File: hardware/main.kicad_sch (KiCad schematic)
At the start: 19 parts, among them J1 Conn_01x04, J2 M300-MV10345M1, J4 ScrewTerminal, J5 ScrewTerminal, J6 ScrewTerminal, K2 ADW11

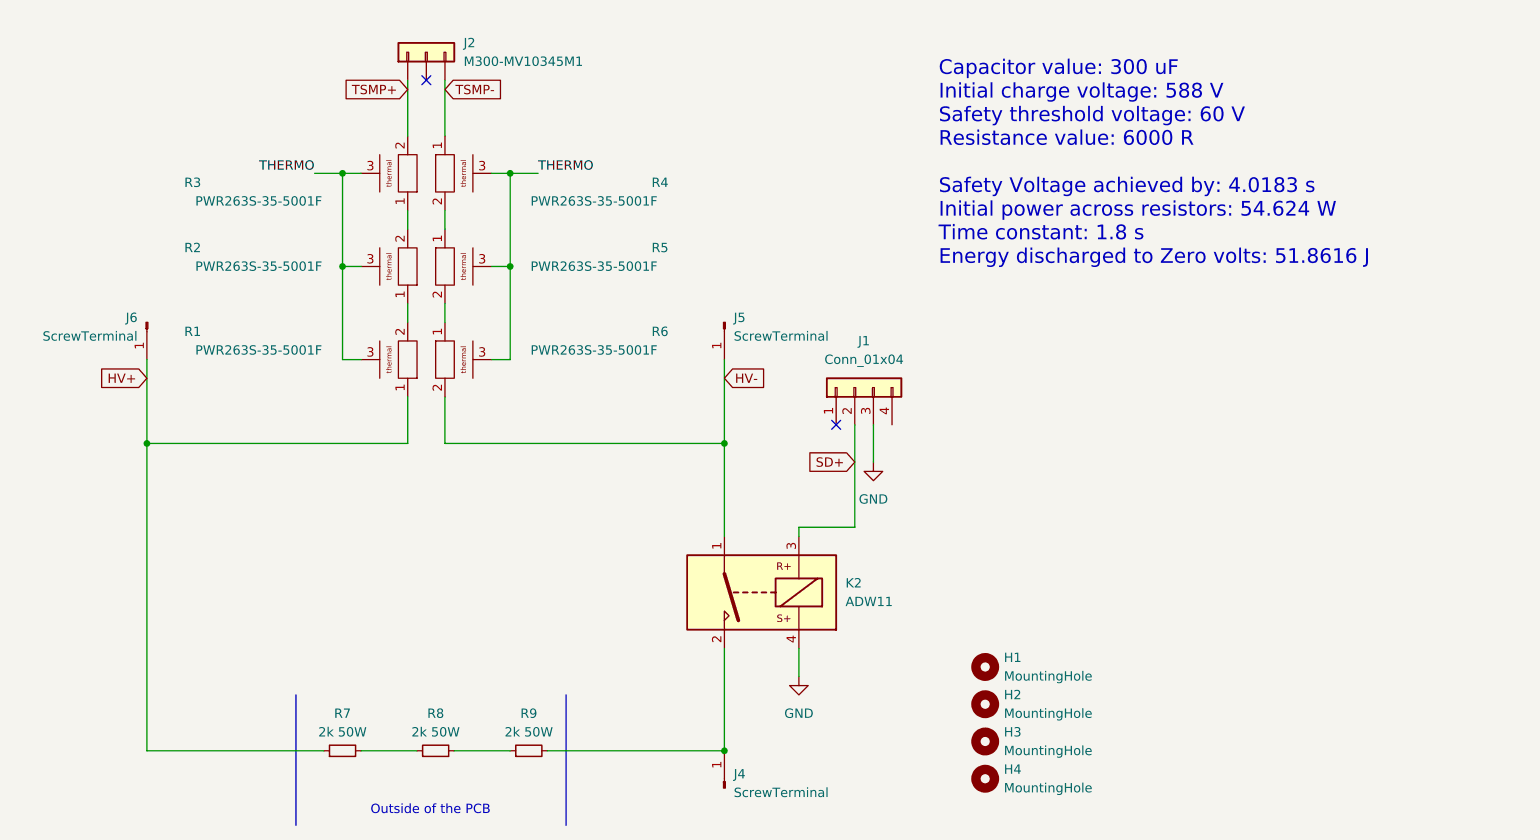
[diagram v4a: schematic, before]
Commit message: Usunięto rezystory discharge z pcb, zmniejszono płytkę
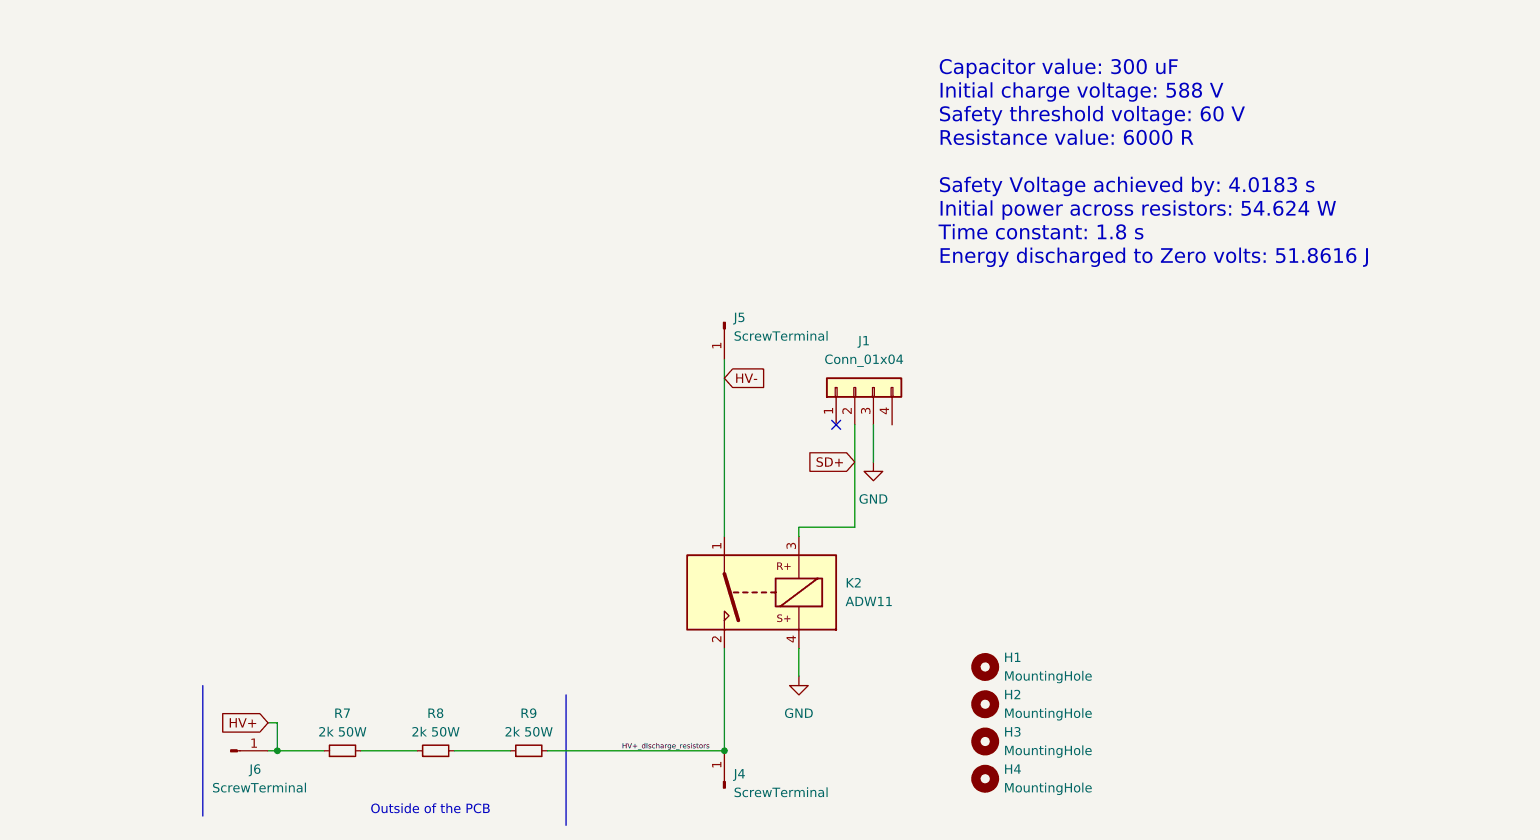
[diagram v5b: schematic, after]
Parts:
- removed J2: M300-MV10345M1, Samacsys:M300MV10345M1, symbol Samacsys_kicad_sym:M300-MV10345M1
- removed R1, R2, R3, R4, R5, R6: PWR263S-35-5001F, 7696:PWR263S-35-5001F, symbol 7696:PWR263S-35-5001F
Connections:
- net HV+_dIscharge_resistors: now reaches J4.1 (Pin_1), K2.2, R9.2
- no-connect marks 2 -> 1
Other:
- moved on the sheet: J6
